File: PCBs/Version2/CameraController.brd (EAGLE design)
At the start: 45 x 46 mm, 30 parts, among them U1 FT232RLSSOP

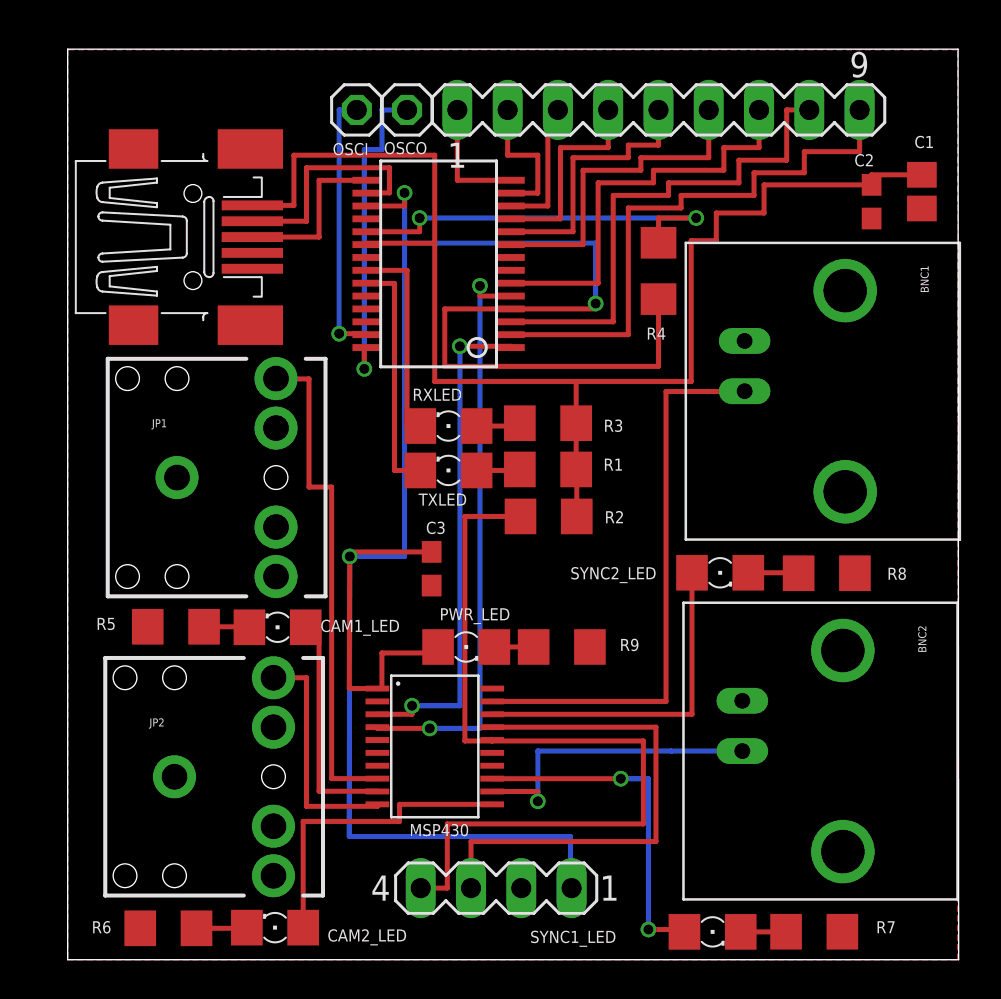
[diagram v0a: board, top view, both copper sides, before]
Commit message: Camera Controller v2
Moved mini USB and audio jacks closer to edge
Added 5 mounting holes onto PCB
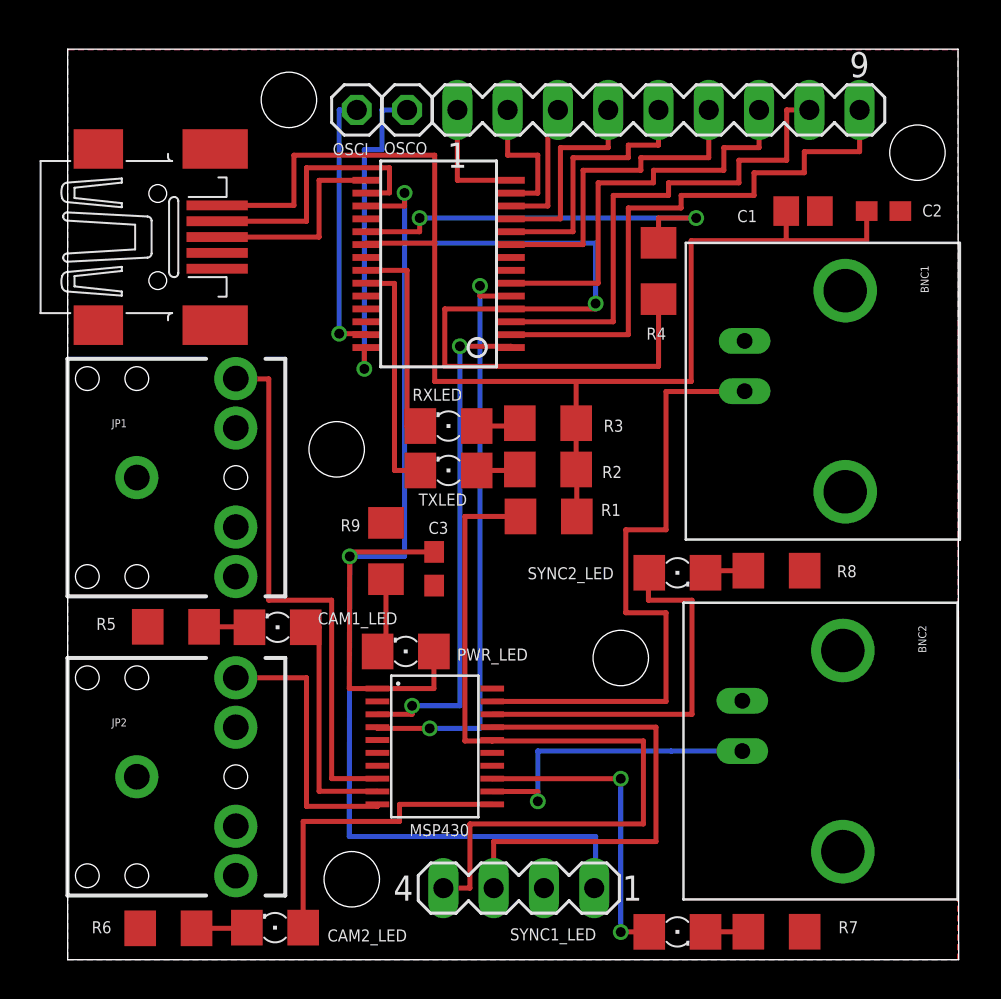
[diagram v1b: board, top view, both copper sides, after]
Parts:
- moved R9 10.1 mm to (16.1, 20.6), turned to 90 degrees
- moved C1 6.08 mm to (37.1, 37.8), turned to 0 degrees
- moved PWR_LED 3.06 mm to (17.1, 15.6), turned to 180 degrees
- moved R8 2.54 mm to (35.8, 19.6)
- moved SYNC2_LED 2.16 mm to (30.8, 19.5)
- moved JP1 2.03 mm to (3.49, 24.4)
- moved R7 1.91 mm to (35.8, 1.41)
- moved JP2 1.90 mm to (3.49, 9.24)
- moved SYNC1_LED 1.78 mm to (30.8, 1.41)
- moved USB_RCPT 1.78 mm to (4.55, 36.5)
- moved PIN_HEADER 1.14 mm to (22.8, 3.62)
- moved C2 0.76 mm to (41.2, 37.8), turned to 0 degrees
- moved C3 0.13 mm to (18.5, 19.7)
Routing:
- net SYNC2: track 28.4 -> 32.5 mm
- net N$8: track 17.2 -> 19.5 mm
- net N$10: track 1.99 -> 4.07 mm
- net CAM1: track 25.3 -> 27.4 mm
- net CAM2: track 11.8 -> 13.7 mm
- net D-: track 12.1 -> 13.9 mm
- net D+: track 8.62 -> 10.4 mm
- net N$6: track 17.5 -> 15.7 mm
- net VCC: track 68.6 -> 67.3 mm
- net RST: track 41.9 -> 40.8 mm
- net TEST: track 25.7 -> 24.6 mm
- net 3V3: track 109.5 -> 110.5 mm
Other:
- board text added: "Camera Controller Version 2 Mini USB Input 2 Audio Jacks, 2 BNC Kemere Lab by Tam Vu"
- board text removed: "Camera Controller Version 1.0 Mini USB Input 2 Audio Jacks, 2 BNC Kemere Lab"
